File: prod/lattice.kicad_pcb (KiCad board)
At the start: 2 copper layers, 102 x 76.5 mm, 70 parts

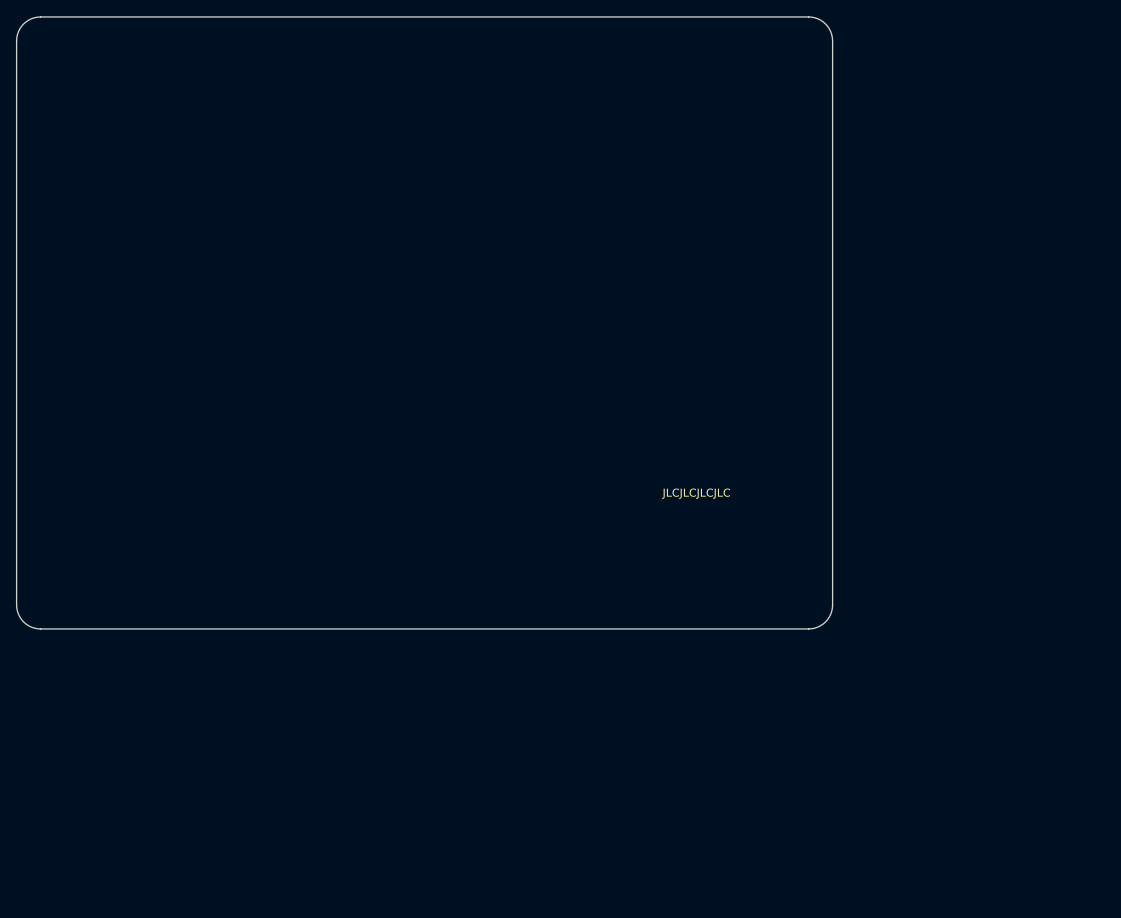
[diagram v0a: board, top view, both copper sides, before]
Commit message: boot button, remove refereence designators, jumper labels
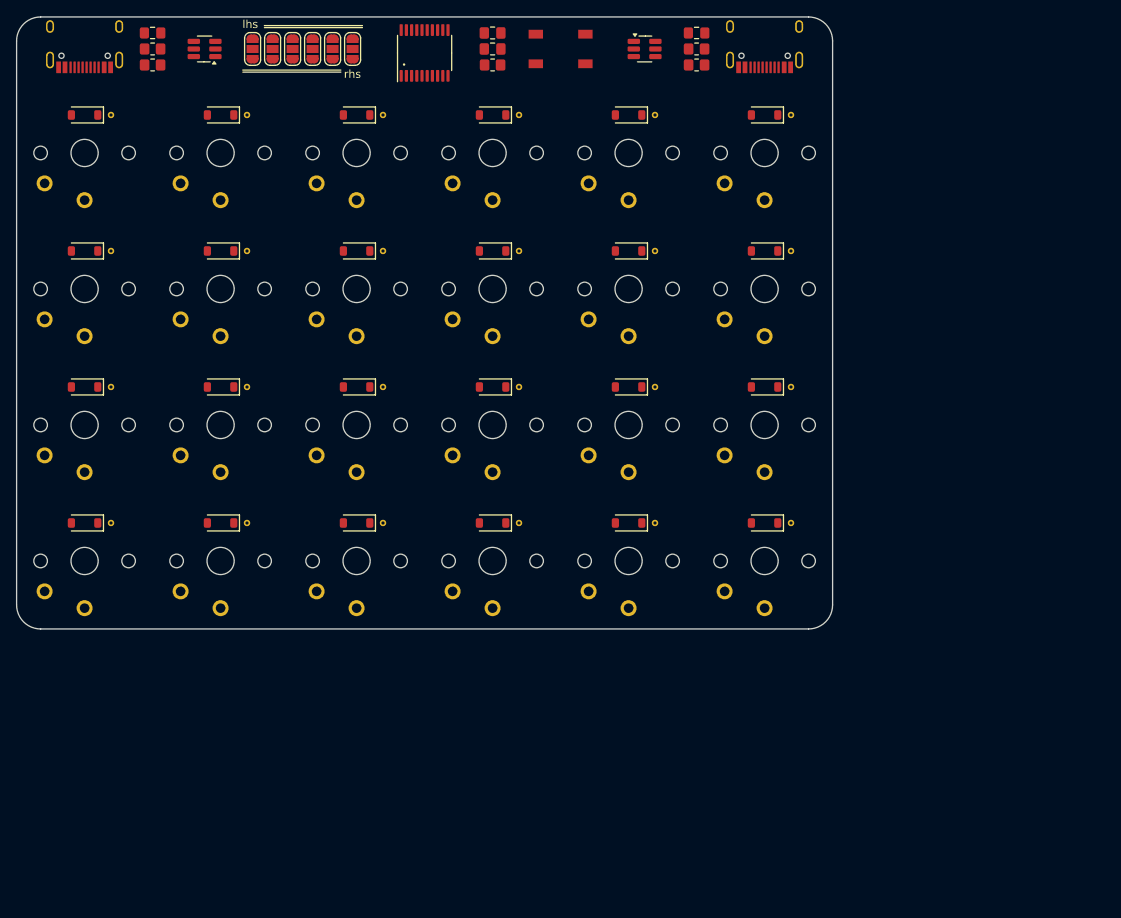
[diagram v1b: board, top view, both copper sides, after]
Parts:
- added REF**: JumperLabels, project:JumperLabels, F.Cu at (112.2, 38.0)
- B1: value (none) -> SW_SPST_SKQG; footprint Pad_1x02 -> project:SW_SPST_SKQG_WithStem
- C1, C2: value (none) -> 100n; footprint 100n -> project:C_0805_2012Metric_Pad1.18x1.45mm_HandSolder
- D1, D10, D11, D12, D13, D14, D15, D16, D17, D18, D19, D2, D20, D21, D22, D23, D24, D3, D4, D5, D6, D7, D8, D9: value (none) -> 1N4148W; footprint 1N4148W -> project:D_SOD-123_via
- F1, F2: value (none) -> 500mA; footprint 500mA -> project:Fuse_0805_2012Metric_Pad1.15x1.40mm_HandSolder
- J1, J2: value (none) -> USB_C_Receptacle; footprint USB_C_Receptacle -> project:USB_C_Receptacle_HRO_TYPE-C-31-M-12
- JP1, JP2, JP3, JP4, JP5, JP6: value (none) -> SolderJumper_3_Open; footprint SolderJumper_3_Open -> project:SolderJumper-3_P1.3mm_Open_RoundedPad1.0x1.5mm
- K1, K10, K11, K12, K13, K14, K15, K16, K17, K18, K19, K2, K20, K21, K22, K23, K24, K3, K4, K5, K6, K7, K8, K9: value (none) -> SW_choc_v1_1u; footprint SW_choc_v1_1u -> project:SW_choc_v1_1u
- R1, R2, R3, R4: value (none) -> 5k1; footprint 5k1 -> project:R_0805_2012Metric_Pad1.20x1.40mm_HandSolder
- R5: value (none) -> 10k; footprint 10k -> project:R_0805_2012Metric_Pad1.20x1.40mm_HandSolder
- SYM1: value (none) -> Logo_Open_Hardware_Small; footprint Logo_Open_Hardware_Small -> project:OSHW-Logo_5.7x6mm_SilkScreen
- U1: value (none) -> CH552T; footprint CH552T -> project:TSSOP-20_4.4x6.5mm_P0.65mm
- U2, U3: value (none) -> USBLC6-2SC6; footprint USBLC6-2SC6 -> project:SOT-23-6_Handsoldering
- moved SYM1 17.0 mm to (161.5, 93.5)
- moved R5 12.7 mm to (136.0, 40.0), turned to 180 degrees
- moved D1 9.50 mm to (85.0, 97.2), turned to 180 degrees
- moved D10 9.50 mm to (119.0, 80.2), turned to 180 degrees
- moved D11 9.50 mm to (119.0, 63.2), turned to 180 degrees
- moved D12 9.50 mm to (119.0, 46.2), turned to 180 degrees
- moved D13 9.50 mm to (136.0, 97.2), turned to 180 degrees
- moved D14 9.50 mm to (136.0, 80.2), turned to 180 degrees
- moved D15 9.50 mm to (136.0, 63.2), turned to 180 degrees
- moved D16 9.50 mm to (136.0, 46.2), turned to 180 degrees
- moved D17 9.50 mm to (153.0, 97.2), turned to 180 degrees
- moved D18 9.50 mm to (153.0, 80.2), turned to 180 degrees
- moved D19 9.50 mm to (153.0, 63.2), turned to 180 degrees
- moved D2 9.50 mm to (85.0, 80.2), turned to 180 degrees
- moved D20 9.50 mm to (153.0, 46.2), turned to 180 degrees
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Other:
- net class Default removed

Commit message: jumper label as footprint
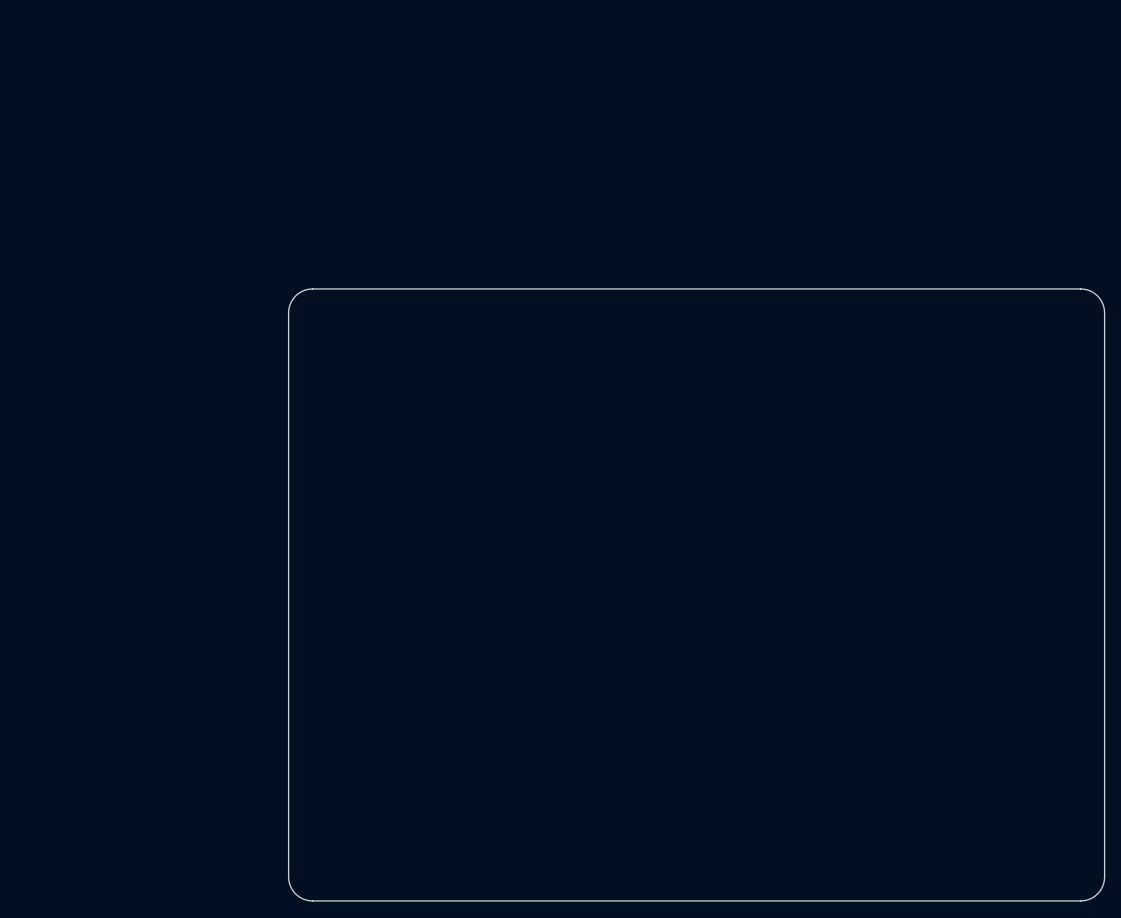
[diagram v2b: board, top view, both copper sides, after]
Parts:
- removed REF**: JumperLabels, project:JumperLabels
- added L1: , SolderJumperLabel, F.Cu at (146.2, 72.0)
- B1: value SW_SPST_SKQG -> (none); footprint project:SW_SPST_SKQG_WithStem -> SW_SPST_SKQG
- C1, C2: value 100n -> (none); footprint project:C_0805_2012Metric_Pad1.18x1.45mm_HandSolder -> 100n
- D1, D10, D11, D12, D13, D14, D15, D16, D17, D18, D19, D2, D20, D21, D22, D23, D24, D3, D4, D5, D6, D7, D8, D9: value 1N4148W -> (none); footprint project:D_SOD-123_via -> 1N4148W
- F1, F2: value 500mA -> (none); footprint project:Fuse_0805_2012Metric_Pad1.15x1.40mm_HandSolder -> 500mA
- J1, J2: value USB_C_Receptacle -> (none); footprint project:USB_C_Receptacle_HRO_TYPE-C-31-M-12 -> USB_C_Receptacle
- JP1, JP2, JP3, JP4, JP5, JP6: value SolderJumper_3_Open -> (none); footprint project:SolderJumper-3_P1.3mm_Open_RoundedPad1.0x1.5mm -> SolderJumper_3_Open
- K1, K10, K11, K12, K13, K14, K15, K16, K17, K18, K19, K2, K20, K21, K22, K23, K24, K3, K4, K5, K6, K7, K8, K9: value SW_choc_v1_1u -> (none); footprint project:SW_choc_v1_1u -> SW_choc_v1_1u
- R1, R2, R3, R4: value 5k1 -> (none); footprint project:R_0805_2012Metric_Pad1.20x1.40mm_HandSolder -> 5k1
- R5: value 10k -> (none); footprint project:R_0805_2012Metric_Pad1.20x1.40mm_HandSolder -> 10k
- SYM1: value Logo_Open_Hardware_Small -> (none); footprint project:OSHW-Logo_5.7x6mm_SilkScreen -> Logo_Open_Hardware_Small
- U1: value CH552T -> (none); footprint project:TSSOP-20_4.4x6.5mm_P0.65mm -> CH552T
- U2, U3: value USBLC6-2SC6 -> (none); footprint project:SOT-23-6_Handsoldering -> USBLC6-2SC6
- moved B1 48.1 mm to (178.5, 72.0)
- moved C1 48.1 mm to (170.0, 70.0)
- moved C2 48.1 mm to (170.0, 72.0)
- moved D1 48.1 mm to (119.0, 131.2)
- moved D10 48.1 mm to (153.0, 114.2)
- moved D11 48.1 mm to (153.0, 97.2)
- moved D12 48.1 mm to (153.0, 80.2)
- moved D13 48.1 mm to (170.0, 131.2)
- moved D14 48.1 mm to (170.0, 114.2)
- moved D15 48.1 mm to (170.0, 97.2)
- moved D16 48.1 mm to (170.0, 80.2)
- moved D17 48.1 mm to (187.0, 131.2)
- moved D18 48.1 mm to (187.0, 114.2)
- moved D19 48.1 mm to (187.0, 97.2)
- moved D2 48.1 mm to (119.0, 114.2)
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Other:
- net class Default added: clearance 0.2, trace_width 0.25, via_dia 0.8, via_drill 0.4
